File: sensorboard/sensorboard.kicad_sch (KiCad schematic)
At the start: 66 parts, among them J10 Conn_01x02_Male, J11 Conn_01x05_Male, J9 Conn_01x02_Male, Q1 MMDT2222A, U1 ESP32-PICO-D4, U2 LTC4411, U3 TPS61092RSAR

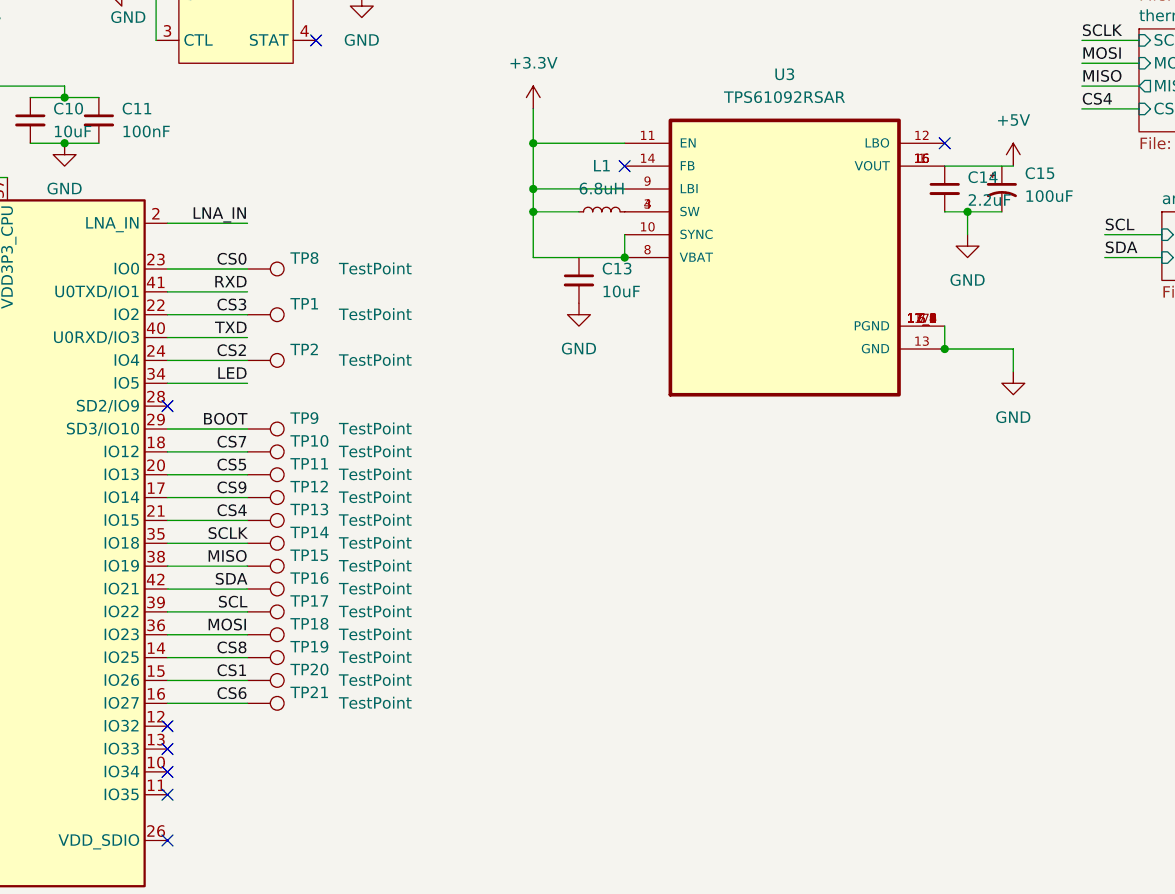
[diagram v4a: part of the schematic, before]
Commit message: LEDs and repositioning for 5V
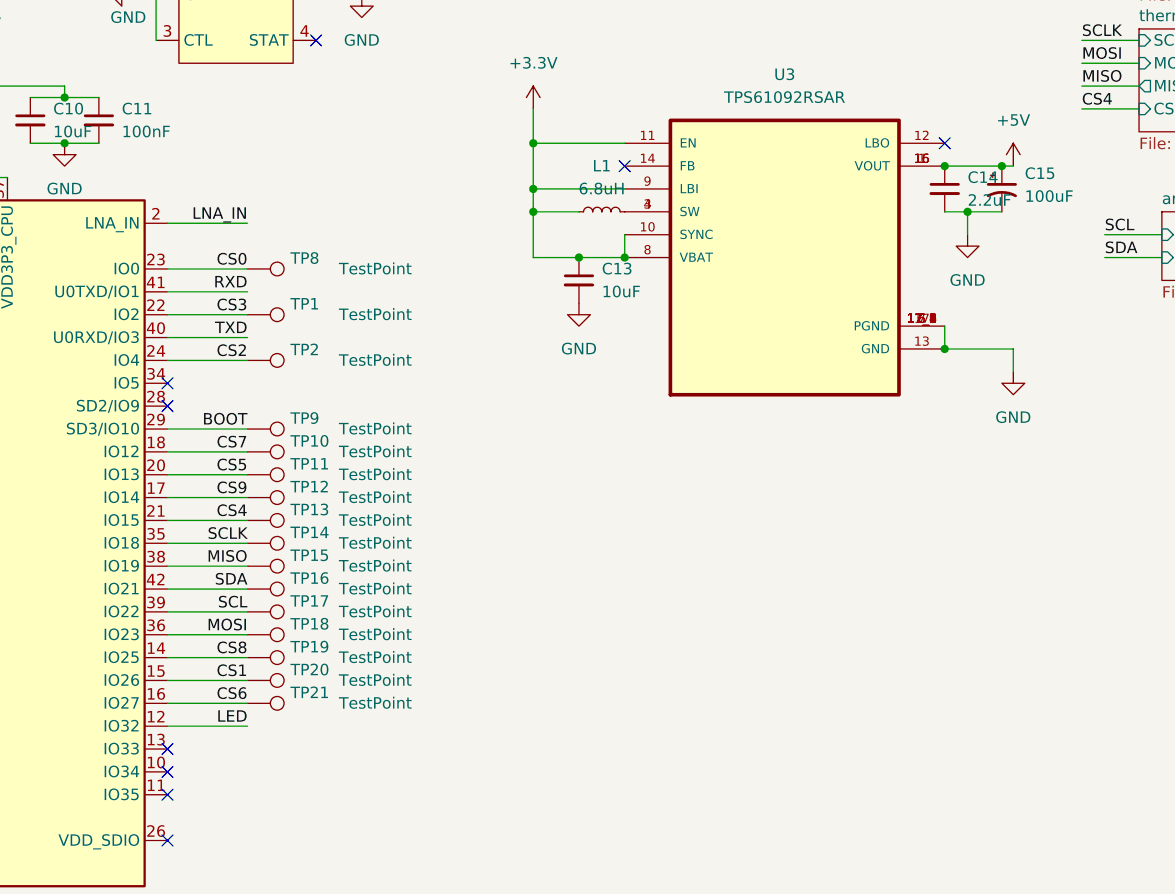
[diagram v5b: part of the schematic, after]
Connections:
- net +3V3: now also C13.1
- net +5V: now also C15.1
- net LED: now also U1.12 (IO32); no longer U1.34 (IO5)
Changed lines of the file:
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@@
   (junction (at 102.87 105.41) (diameter 0) (color 0 0 0 0)
   )
+  (junction (at 170.18 114.3) (diameter 0) (color 0 0 0 0)
+  )
   (junction (at 165.1 101.6) (diameter 0) (color 0 0 0 0)
   )
@@
   (junction (at 33.02 25.4) (diameter 0) (color 0 0 0 0)
   )
+  (junction (at 210.82 104.14) (diameter 0) (color 0 0 0 0)
+  )
   (junction (at 113.03 101.6) (diameter 0) (color 0 0 0 0)
   )
@@
   )
   (junction (at 175.26 114.3) (diameter 0) (color 0 0 0 0)
+  )
+  (junction (at 217.17 104.14) (diameter 0) (color 0 0 0 0)
   )
   (junction (at 186.69 39.37) (diameter 0) (color 0 0 0 0)
@@
   (no_connect (at 124.46 130.81))
   (no_connect (at 210.82 101.6))
+  (no_connect (at 124.46 128.27))
   (no_connect (at 124.46 179.07))
   (no_connect (at 124.46 173.99))
@@
   (no_connect (at 83.82 151.13))
   (no_connect (at 276.86 59.69))
-  (no_connect (at 124.46 166.37))
   (no_connect (at 124.46 168.91))
   (no_connect (at 83.82 120.65))
@@
     (stroke (width 0) (type default) (color 0 0 0 0))
   )
-  (wire (pts (xy 124.46 128.27) (xy 133.35 128.27))
-    (stroke (width 0) (type default) (color 0 0 0 0))
-  )
   (wire (pts (xy 124.46 163.83) (xy 133.35 163.83))
     (stroke (width 0) (type default) (color 0 0 0 0))
@@
     (stroke (width 0) (type default) (color 0 0 0 0))
   )
-  (wire (pts (xy 165.1 114.3) (xy 175.26 114.3))
-    (stroke (width 0) (type default) (color 0 0 0 0))
-  )
   (wire (pts (xy 254 57.15) (xy 260.35 57.15))
     (stroke (width 0) (type default) (color 0 0 0 0))
@@
     (stroke (width 0) (type default) (color 0 0 0 0))
   )
+  (wire (pts (xy 165.1 114.3) (xy 170.18 114.3))
+    (stroke (width 0) (type default) (color 0 0 0 0))
+  )
   (wire (pts (xy 96.52 25.4) (xy 96.52 30.48))
     (stroke (width 0) (type default) (color 0 0 0 0))
@@
     (stroke (width 0) (type default) (color 0 0 0 0))
   )
+  (wire (pts (xy 217.17 104.14) (xy 218.44 104.14))
+    (stroke (width 0) (type default) (color 0 0 0 0))
+  )
   (wire (pts (xy 226.06 76.2) (xy 232.41 76.2))
     (stroke (width 0) (type default) (color 0 0 0 0))
@@
     (stroke (width 0) (type default) (color 0 0 0 0))
   )
-  (wire (pts (xy 210.82 104.14) (xy 218.44 104.14))
+  (wire (pts (xy 210.82 104.14) (xy 217.17 104.14))
     (stroke (width 0) (type default) (color 0 0 0 0))
   )
@@
     (stroke (width 0) (type default) (color 0 0 0 0))
   )
+  (wire (pts (xy 170.18 114.3) (xy 175.26 114.3))
+    (stroke (width 0) (type default) (color 0 0 0 0))
+  )
   (wire (pts (xy 30.48 191.77) (xy 30.48 190.5))
     (stroke (width 0) (type default) (color 0 0 0 0))
@@
   )
   (wire (pts (xy 124.46 125.73) (xy 133.35 125.73))
+    (stroke (width 0) (type default) (color 0 0 0 0))
+  )
+  (wire (pts (xy 124.46 166.37) (xy 133.35 166.37))
     (stroke (width 0) (type default) (color 0 0 0 0))
   )
@@
     (effects (font (size 1.27 1.27)) (justify right bottom))
   )
-  (label "LED" (at 133.35 128.27 180)
-    (effects (font (size 1.27 1.27)) (justify right bottom))
-  )
+  (label "LED" (at 133.35 166.37 180)
+    (effects (font (size 1.27 1.27)) (justify right bottom))
+  )

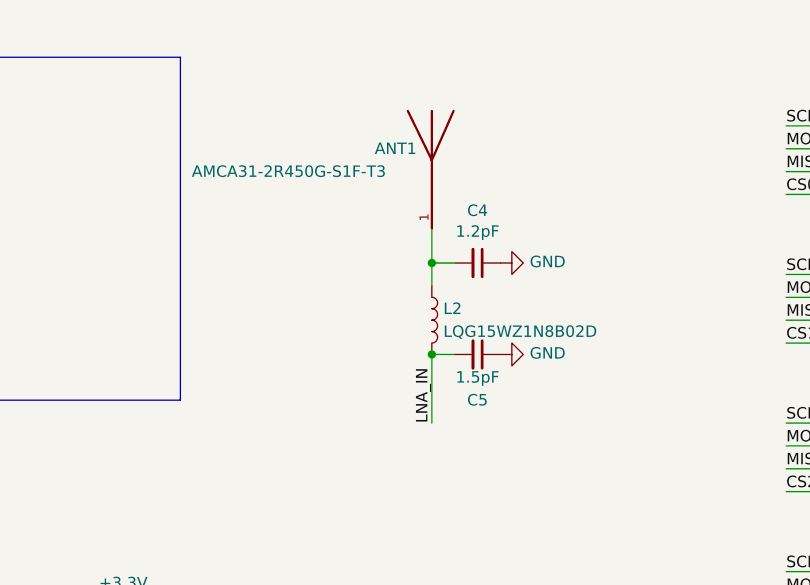
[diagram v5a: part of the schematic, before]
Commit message: Swapped the antenna for the coaxial connector
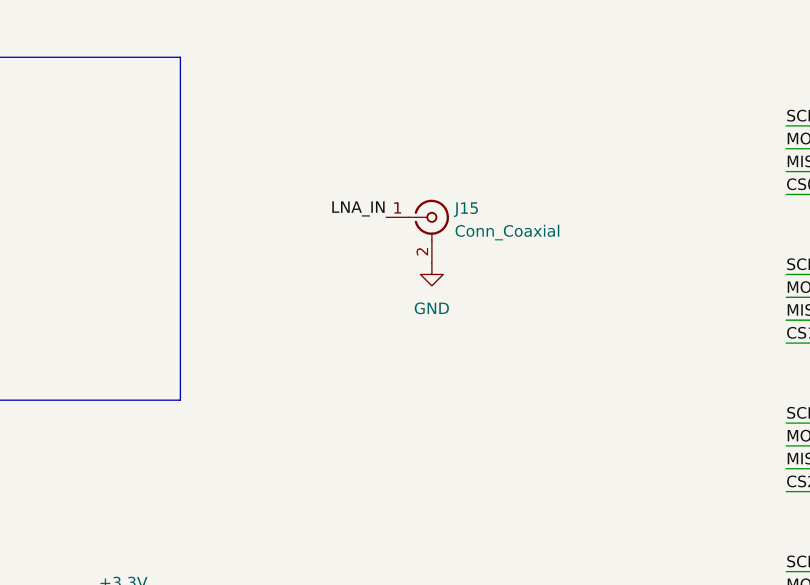
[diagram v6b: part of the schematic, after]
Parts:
- removed ANT1: AMCA31-2R450G-S1F-T3, iclr:ANT_AMCA31-2R450G-S1F-T3, symbol AMCA31-2R450G-S1F-T3:AMCA31-2R450G-S1F-T3
- removed C4: 1.2pF, Capacitor_SMD:C_0603_1608Metric, symbol Device:C_Small
- removed C5: 1.5pF, Capacitor_SMD:C_0603_1608Metric, symbol Device:C_Small
- removed L2: LQG15WZ1N8B02D, iclr:INDC1006X60N, symbol Device:L
- added J15: Conn_Coaxial, Connector_Coaxial:U.FL_Molex_MCRF_73412-0110_Vertical, symbol Connector:Conn_Coaxial
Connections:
- net GND: now also J15.2 (Ext)
- net LNA_IN: now also J15.1 (In)

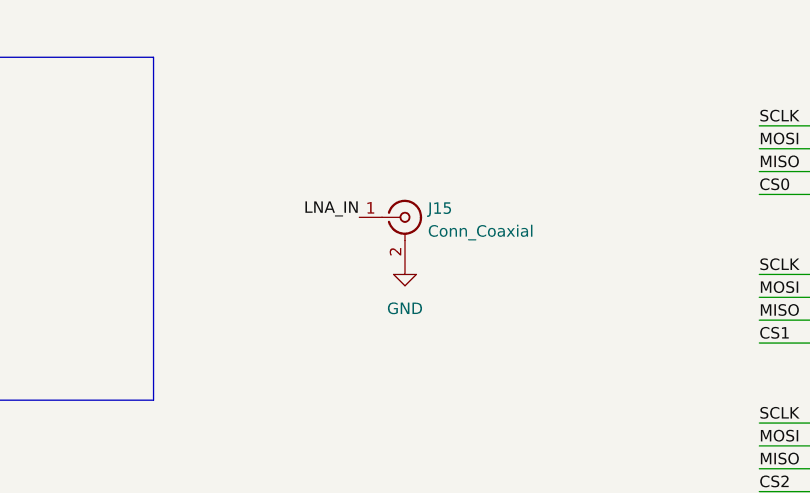
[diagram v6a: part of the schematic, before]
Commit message: Change 3.3V, added curved edges
changed the copy, added keepout for UFL connector
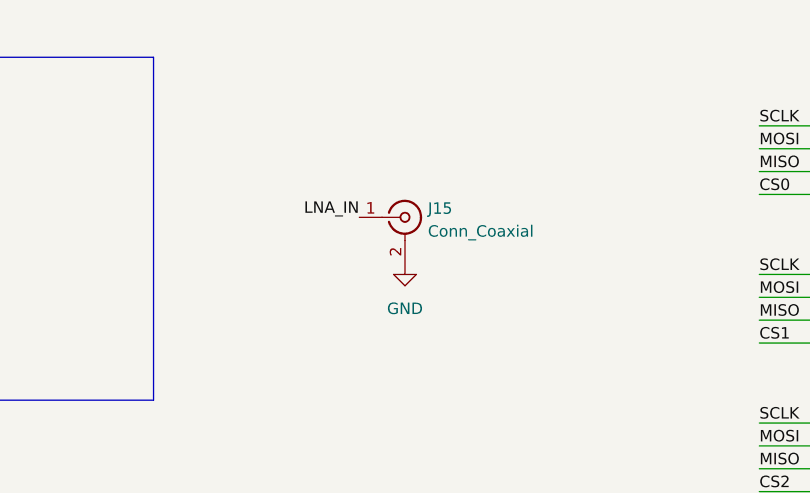
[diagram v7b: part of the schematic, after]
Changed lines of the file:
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@@
       (effects (font (size 1.27 1.27)) hide)
     )
-    (property "Datasheet" " ~" (id 3) (at 186.69 34.29 0)
+    (property "Datasheet" "https://docs.rs-online.com/332c/0900766b813c49d5.pdf" (id 3) (at 186.69 34.29 0)
       (effects (font (size 1.27 1.27)) hide)
     )
